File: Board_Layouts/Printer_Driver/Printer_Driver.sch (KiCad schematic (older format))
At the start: 33 parts, among them J1 USB_B, J2 Conn_01x06, J3 Conn_01x03, J4 DB25_Female_MountingHoles, J5 8P8C, U1 FT230XS, U2 PIC16F1503-IP, U3 74HC595, U4 PCA9615

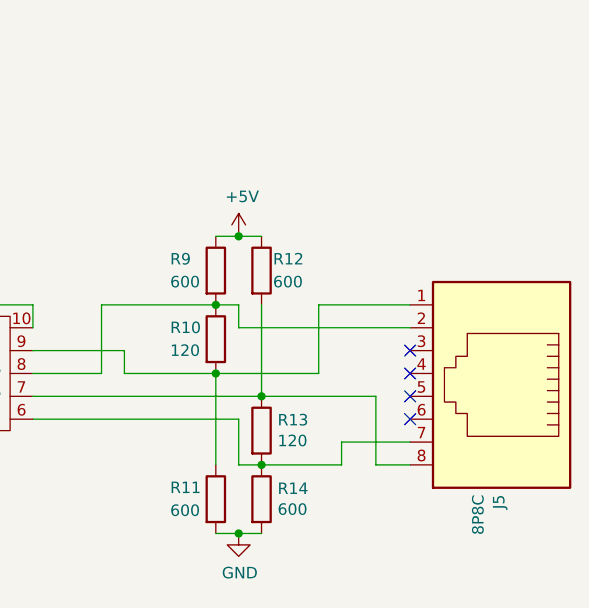
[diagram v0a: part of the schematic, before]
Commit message: Update local changes & working on printer driver
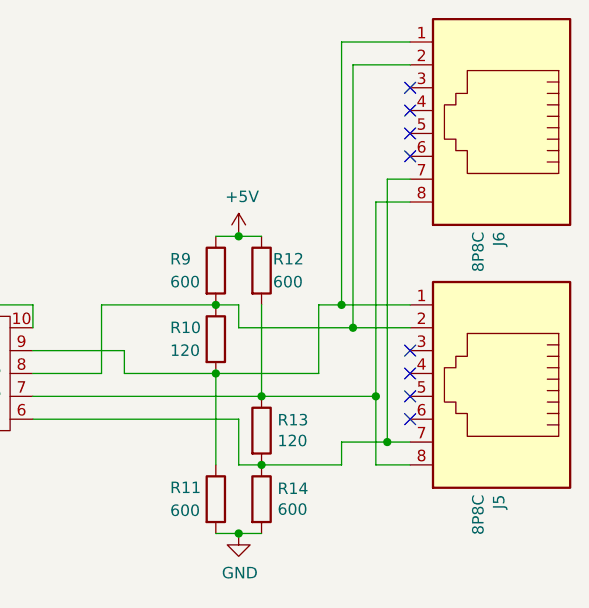
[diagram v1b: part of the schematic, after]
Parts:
- added J6: 8P8C, Connector_RJ:RJ45_Amphenol_54602-x08_Horizontal, symbol Connector:8P8C
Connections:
- net at J5.1, R10.2, R11.1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: now also J6.1
- net at J5.2, R10.1, R9.2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: now also J6.2
- net at J5.7, R13.2, R14.1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: now also J6.7
- net at J5.8, R12.2, R13.1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: now also J6.8
- no-connect marks 18 -> 22
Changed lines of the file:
@@
 EESchema Schematic File Version 4
-LIBS:Printer Driver-cache
+LIBS:Printer_Driver-cache
 EELAYER 29 0
 EELAYER END
@@
 	13600 2000 13700 2000
 Wire Wire Line
-	13700 2400 14450 2400
+	13700 2400 14200 2400
 Wire Wire Line
 	13700 2300 13700 2400
@@
 	13600 2300 13700 2300
 Wire Wire Line
-	14050 2300 14450 2300
+	14050 2300 14150 2300
 Wire Wire Line
 	14050 2600 14050 2300
@@
 	14150 2900 14150 3000
 Wire Wire Line
-	14450 2900 14150 2900
+	14450 2900 14350 2900
 Wire Wire Line
 	14300 3000 14450 3000
@@
 Wire Wire Line
 	11800 2500 11800 4600
+$Comp
+L Connector:8P8C J6
+U 1 1 5D901381
+P 14850 1450
+F 0 "J6" V 14861 1980 50  0000 L CNN
+F 1 "8P8C" V 14952 1980 50  0000 L CNN
+F 2 "Connector_RJ:RJ45_Amphenol_54602-x08_Horizontal" V 14850 1475 50  0001 C CNN
+F 3 "~" V 14850 1475 50  0001 C CNN
+	1    14850 1450
+	-1   0    0    1
+$EndComp
+NoConn ~ 14450 1350
+NoConn ~ 14450 1450
+NoConn ~ 14450 1550
+NoConn ~ 14450 1650
+Wire Wire Line
+	14450 1150 14150 1150
+Wire Wire Line
+	14150 1150 14150 2300
+Connection ~ 14150 2300
+Wire Wire Line
+	14150 2300 14450 2300
+Wire Wire Line
+	14300 2700 14300 1850
+Wire Wire Line
+	14300 1850 14450 1850
+Connection ~ 14300 2700
+Wire Wire Line
+	14350 2900 14350 1750
+Wire Wire Line
+	14350 1750 14450 1750
+Connection ~ 14350 2900
+Wire Wire Line
+	14350 2900 14150 2900
+Wire Wire Line
+	14200 2400 14200 1250
+Wire Wire Line
+	14200 1250 14450 1250
+Connection ~ 14200 2400
+Wire Wire Line
+	14200 2400 14450 2400
 $EndSCHEMATC
